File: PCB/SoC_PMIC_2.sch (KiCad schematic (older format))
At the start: 1 part

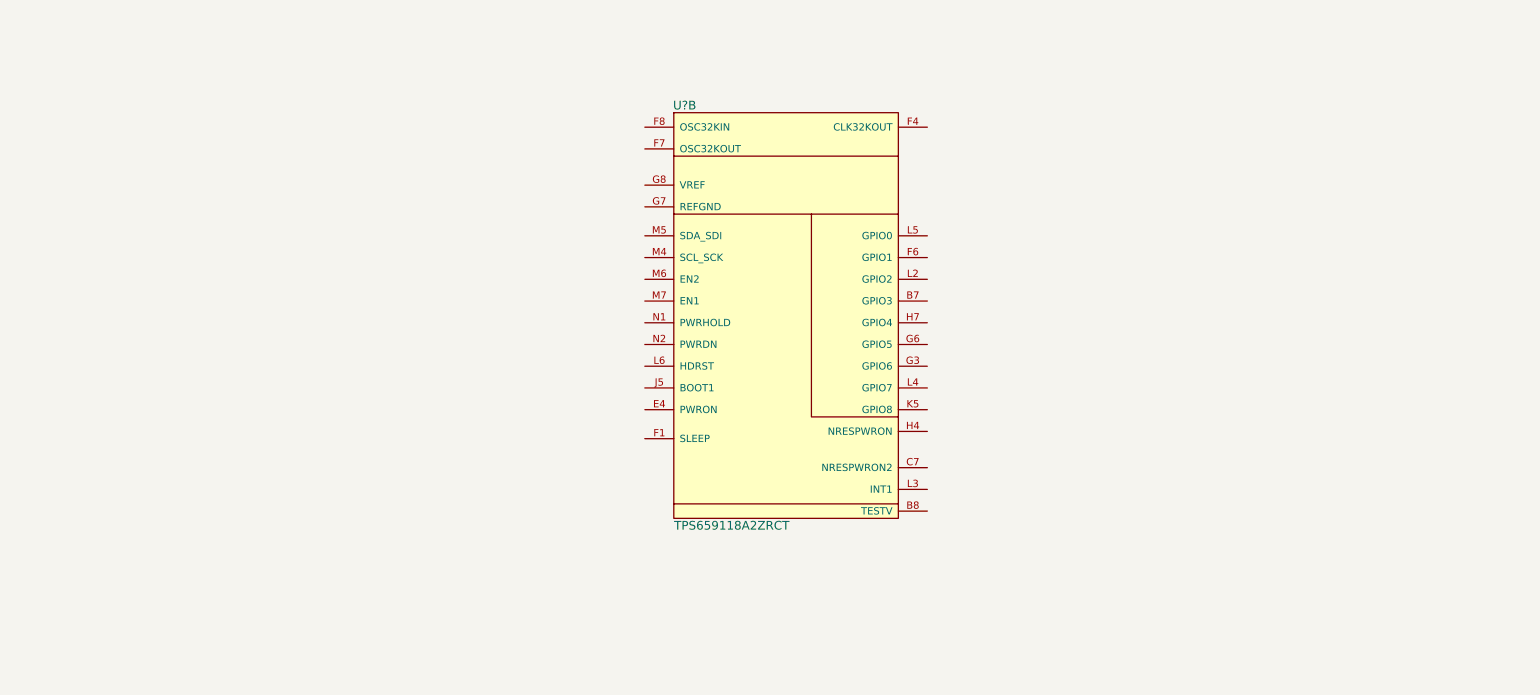
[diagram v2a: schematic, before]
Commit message: Schematic Progress
More progress on schematic. Image sensor schematic nearly finished, need
to check termination requirements of signals. Memory schematic nearly
solidified. LDO added to image sensor circuit for analog supply (3V).
Need to research termination requirements for memory as well. Need to
check what internal termination if any resistors are available in the
Zynq soc.
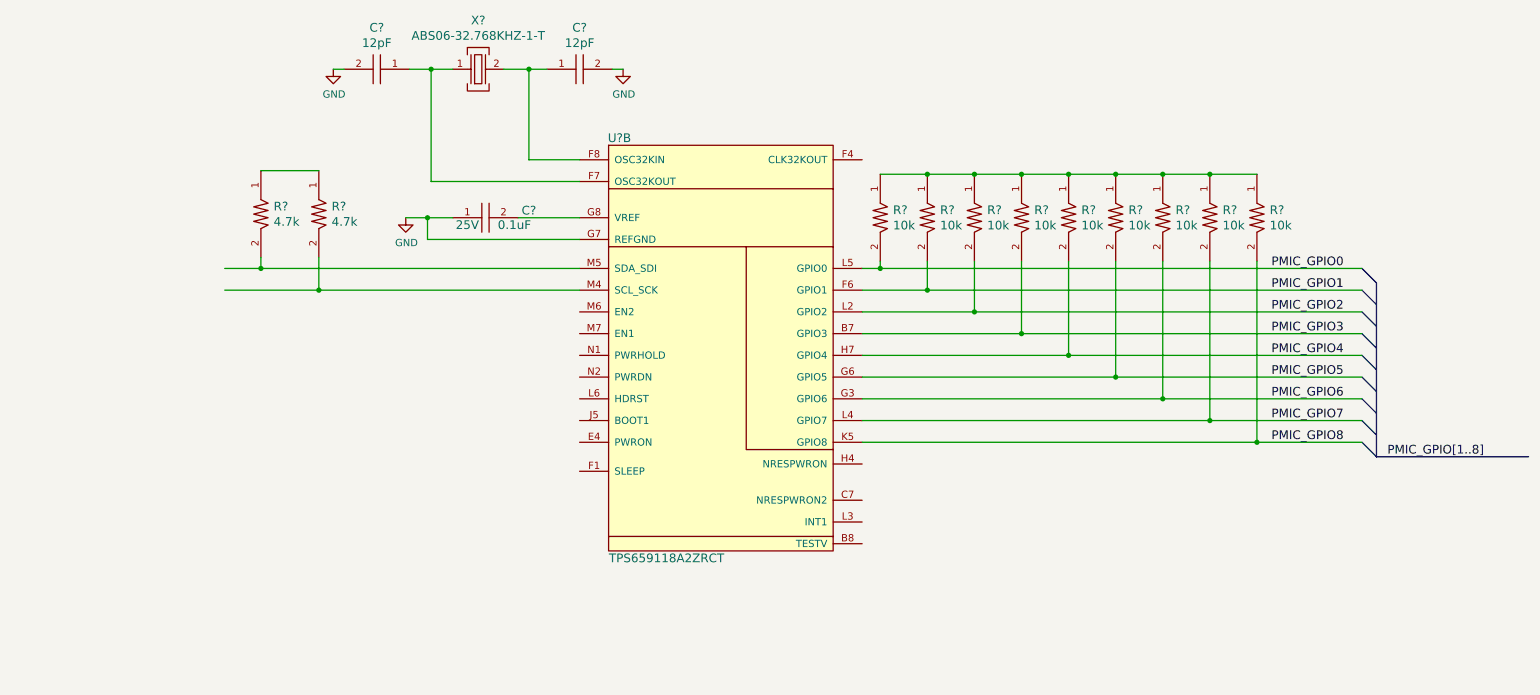
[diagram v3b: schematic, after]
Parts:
- added C? (x2): CL10C120FB8NNNC, PCB_Footprints:C0603, symbol CL10C120FB8NNNC
- added C?: 08053C104JAT2A, PCB_Footprints:C0805, symbol 08053C104JAT2A
- added R? (x9): RC1005F103CS, PCB_Footprints:R0402, symbol RC1005F103CS
- added R? (x2): RC1005F472CS, PCB_Footprints:R0402, symbol RC1005F472CS
- added X?: ABS06-32.768KHZ-1-T, PCB_Footprints:ABS06-32.768KHZ-1-T, symbol ABS06-32.768KHZ-1-T
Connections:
- net labels added: GND, PMIC_GPIO0, PMIC_GPIO1, PMIC_GPIO2, PMIC_GPIO3, PMIC_GPIO4, PMIC_GPIO5, PMIC_GPIO6, PMIC_GPIO7, PMIC_GPIO8, PMIC_GPIO[1..8]
- wire segments 0 -> 36
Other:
- moved on the sheet: U?B

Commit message: Memory and Camera
Memory and Camera schematics tentatively complete. They are subject to
change as all hardware projects are.
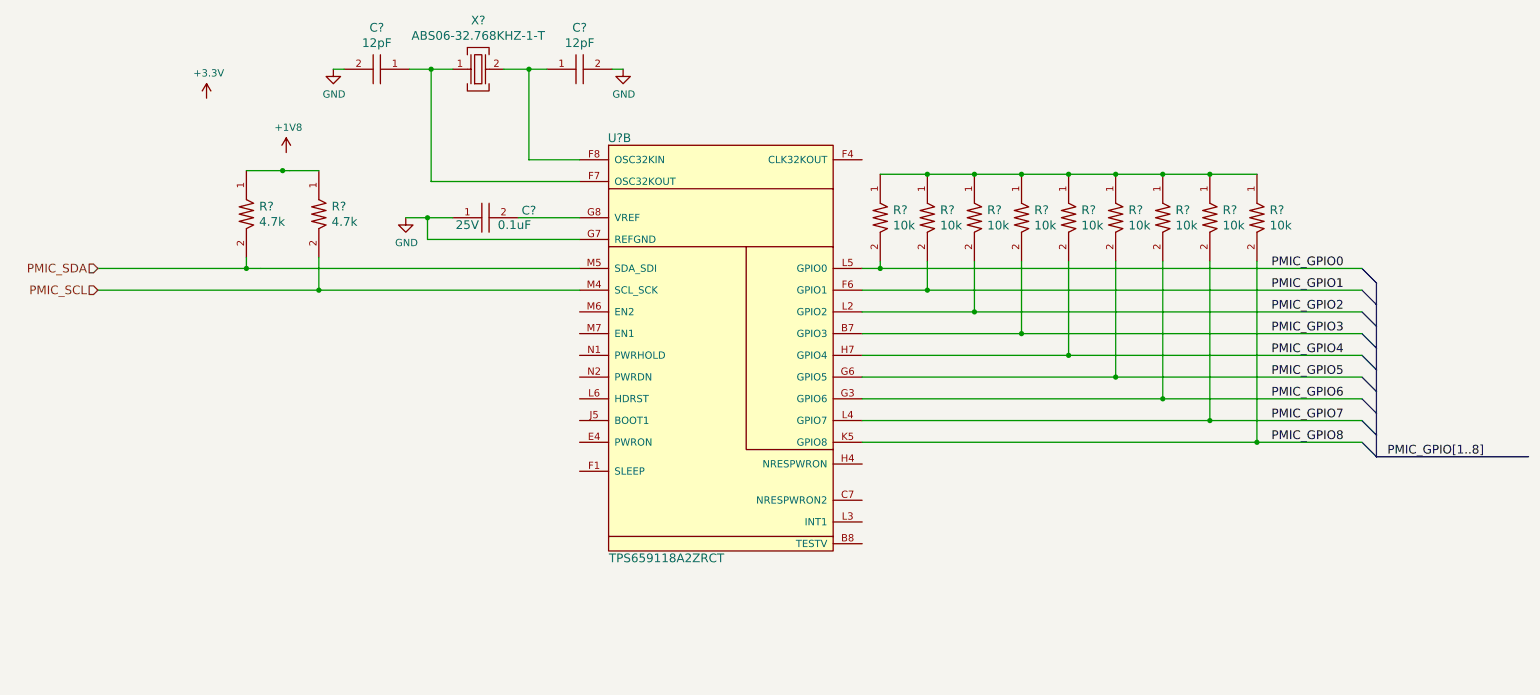
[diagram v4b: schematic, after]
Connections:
- net labels added: +1V8, +3.3V, PMIC_SCL, PMIC_SDA
- wire segments 36 -> 60
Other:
- moved on the sheet: R?
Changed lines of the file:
@@
 $Descr A4 11693 8268
 encoding utf-8
-Sheet 9 9
+Sheet 9 8
 Title ""
 Date ""
@@
 $EndComp
 Wire Wire Line
-	3800 2100 4100 2100
-Wire Wire Line
-	3150 2100 3450 2100
+	3800 2100 3975 2100
+Wire Wire Line
+	3975 2100 4100 2100
+Wire Wire Line
+	3150 2100 3300 2100
+Wire Wire Line
+	3300 2100 3450 2100
 Wire Wire Line
 	2625 2100 2700 2100
@@
 	3275 3275 4325 3275
 Wire Wire Line
-	3125 3125 3450 3125
+	3125 3125 3275 3125
+Wire Wire Line
+	3275 3125 3450 3125
 Wire Wire Line
 	3275 3275 3275 3125
 Connection ~ 3275 3125
 Wire Wire Line
-	4325 3475 1875 3475
-Wire Wire Line
-	4325 3625 1875 3625
-Wire Wire Line
-	6275 3475 9725 3475
-Wire Wire Line
-	6275 3625 9725 3625
-Wire Wire Line
-	6275 3775 9725 3775
-Wire Wire Line
-	6275 3925 9725 3925
-Wire Wire Line
-	6275 4075 9725 4075
-Wire Wire Line
-	6275 4225 9725 4225
-Wire Wire Line
-	6275 4375 9725 4375
-Wire Wire Line
-	6275 4525 9725 4525
-Wire Wire Line
-	6275 4675 9725 4675
+	4325 3475 2125 3475
+Wire Wire Line
+	2125 3475 2025 3475
+Wire Wire Line
+	2025 3475 1000 3475
+Wire Wire Line
+	4325 3625 2525 3625
+Wire Wire Line
+	2525 3625 1000 3625
+Wire Wire Line
+	6275 3475 6400 3475
+Wire Wire Line
+	6400 3475 9725 3475
+Wire Wire Line
+	6275 3625 6725 3625
+Wire Wire Line
+	6725 3625 9725 3625
+Wire Wire Line
+	6275 3775 7050 3775
+Wire Wire Line
+	7050 3775 9725 3775
+Wire Wire Line
+	6275 3925 7375 3925
+Wire Wire Line
+	7375 3925 9725 3925
+Wire Wire Line
+	6275 4075 7700 4075
+Wire Wire Line
+	7700 4075 9725 4075
+Wire Wire Line
+	6275 4225 8025 4225
+Wire Wire Line
+	8025 4225 9725 4225
+Wire Wire Line
+	6275 4375 8350 4375
+Wire Wire Line
+	8350 4375 9725 4375
+Wire Wire Line
+	6275 4525 8675 4525
+Wire Wire Line
+	8675 4525 9725 4525
+Wire Wire Line
+	6275 4675 9000 4675
+Wire Wire Line
+	9000 4675 9725 4675
 Wire Wire Line
 	6400 3425 6400 3475
@@
 Connection ~ 9000 4675
 Wire Wire Line
-	6400 2825 9000 2825
+	6400 2825 6725 2825
+Wire Wire Line
+	6725 2825 7050 2825
+Wire Wire Line
+	7050 2825 7375 2825
+Wire Wire Line
+	7375 2825 7700 2825
+Wire Wire Line
+	7700 2825 8025 2825
+Wire Wire Line
+	8025 2825 8350 2825
+Wire Wire Line
+	8350 2825 8675 2825
+Wire Wire Line
+	8675 2825 9000 2825
 Connection ~ 8675 2825
 Connection ~ 8350 2825
@@
 	9725 4675 9825 4775
 Wire Bus Line
-	9825 3575 9825 4775
+	9825 3575 9825 3725
+Wire Bus Line
+	9825 3725 9825 3875
+Wire Bus Line
+	9825 3875 9825 4025
+Wire Bus Line
+	9825 4025 9825 4175
+Wire Bus Line
+	9825 4175 9825 4325
+Wire Bus Line
+	9825 4325 9825 4475
+Wire Bus Line
+	9825 4475 9825 4625
+Wire Bus Line
+	9825 4625 9825 4775
 Wire Bus Line
 	9825 4775 10875 4775
@@
 L RC1005F472CS R?
 U 1 1 588E2FC1
-P 2125 3100
-F 0 "R?" V 2072 3188 60  0000 L CNN
-F 1 "RC1005F472CS" H 2125 3347 60  0001 C CNN
-F 2 "PCB_Footprints:R0402" H 1725 3350 60  0001 C CNN
-F 3 "https://media.digikey.com/pdf/Data%20Sheets/Samsung%20PDFs/RC_Series_ds.pdf" H 1825 3550 60  0001 C CNN
-F 4 "0.00173 @ 5000" H 3675 5050 60  0001 C CNN "Cost"
-F 5 "5 Sept 2016" H 2025 3650 60  0001 C CNN "Date Created"
-F 6 "5 Sept 2016" H 2125 3750 60  0001 C CNN "Date Modified"
-F 7 "Adam Vadala-Roth" H 2225 3850 60  0001 C CNN "Designer"
-F 8 "0.4mm" H 2325 3950 60  0001 C CNN "Height"
-F 9 "Yes" H 2425 4050 60  0001 C CNN "RHoS?"
-F 10 "Samsung Electro-Mechanics America, Inc." H 2525 4150 60  0001 C CNN "MFR"
-F 11 "RC1005F472CS" H 2625 4250 60  0001 C CNN "MFR#"
-F 12 "SMT/SMD" H 2725 4350 60  0001 C CNN "Mounting"
-F 13 "2" H 2825 4450 60  0001 C CNN "Pin Count#"
-F 14 "Active" H 2925 4550 60  0001 C CNN "Status"
-F 15 "1%" H 3025 4650 60  0001 C CNN "Tolerance"
-F 16 "passive" H 3125 4750 60  0001 C CNN "Type"
-F 17 "N/A" H 3225 4850 60  0001 C CNN "Voltage"
-F 18 "1/16" H 3325 4950 60  0001 C CNN "Wattage"
-F 19 "4.7k" V 2178 3188 60  0000 L CNN "Component-Value"
-F 20 "RES SMD 4.7K OHM 1% 1/16W 0402" H 3525 5150 60  0001 C CNN "Description"
-	1    2125 3100
+P 2025 3100
+F 0 "R?" V 1972 3188 60  0000 L CNN
+F 1 "RC1005F472CS" H 2025 3347 60  0001 C CNN
+F 2 "PCB_Footprints:R0402" H 1625 3350 60  0001 C CNN
+F 3 "https://media.digikey.com/pdf/Data%20Sheets/Samsung%20PDFs/RC_Series_ds.pdf" H 1725 3550 60  0001 C CNN
+F 4 "0.00173 @ 5000" H 3575 5050 60  0001 C CNN "Cost"
+F 5 "5 Sept 2016" H 1925 3650 60  0001 C CNN "Date Created"
+F 6 "5 Sept 2016" H 2025 3750 60  0001 C CNN "Date Modified"
+F 7 "Adam Vadala-Roth" H 2125 3850 60  0001 C CNN "Designer"
+F 8 "0.4mm" H 2225 3950 60  0001 C CNN "Height"
+F 9 "Yes" H 2325 4050 60  0001 C CNN "RHoS?"
+F 10 "Samsung Electro-Mechanics America, Inc." H 2425 4150 60  0001 C CNN "MFR"
+F 11 "RC1005F472CS" H 2525 4250 60  0001 C CNN "MFR#"
+F 12 "SMT/SMD" H 2625 4350 60  0001 C CNN "Mounting"
+F 13 "2" H 2725 4450 60  0001 C CNN "Pin Count#"
+F 14 "Active" H 2825 4550 60  0001 C CNN "Status"
+F 15 "1%" H 2925 4650 60  0001 C CNN "Tolerance"
+F 16 "passive" H 3025 4750 60  0001 C CNN "Type"
+F 17 "N/A" H 3125 4850 60  0001 C CNN "Voltage"
+F 18 "1/16" H 3225 4950 60  0001 C CNN "Wattage"
+F 19 "4.7k" V 2078 3188 60  0000 L CNN "Component-Value"
+F 20 "RES SMD 4.7K OHM 1% 1/16W 0402" H 3425 5150 60  0001 C CNN "Description"
+	1    2025 3100
 	0    1    1    0
 $EndComp
@@
 $EndComp
 Wire Wire Line
-	2125 3400 2125 3475
-Connection ~ 2125 3475
+	2025 3400 2025 3475
+Connection ~ 2025 3475
 Wire Wire Line
 	2525 3400 2525 3625
 Connection ~ 2525 3625
 Wire Wire Line
-	2125 2800 2525 2800
+	2025 2800 2275 2800
+Wire Wire Line
+	2275 2800 2325 2800
+Wire Wire Line
+	2325 2800 2525 2800
+Text HLabel 1000 3475 0    60   Input ~ 0
+PMIC_SDA
+Text HLabel 1000 3625 0    60   Input ~ 0
+PMIC_SCL
+$Comp
+L +3.3V #PWR?
+U 1 1 588E5DBF
+P 1750 2300
+F 0 "#PWR?" H 1750 2150 50  0001 C CNN
+F 1 "+3.3V" H 1765 2473 50  0000 C CNN
+F 2 "" H 1750 2300 50  0001 C CNN
+F 3 "" H 1750 2300 50  0001 C CNN
+	1    1750 2300
+	1    0    0    -1
+$EndComp
+Connection ~ 2275 2800
+$Comp
+L +1V8 #PWR?
+U 1 1 588EDED9
+P 2300 2675
+F 0 "#PWR?" H 2300 2525 50  0001 C CNN
+F 1 "+1V8" H 2315 2848 50  0000 C CNN
+F 2 "" H 2300 2675 50  0001 C CNN
+F 3 "" H 2300 2675 50  0001 C CNN
+	1    2300 2675
+	1    0    0    -1
+$EndComp
 $EndSCHEMATC

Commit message: USB
This commit contains mostly work done to the USB sections. Theres a FTDI
chip for USB coms and programmign and an USB transceiver/PHY for usb
perfipherals or daisychaining devices.  Also the termiantion resistors
have been removed from the memory since termination can be set on DDR
pins of the FPGA with verilog.
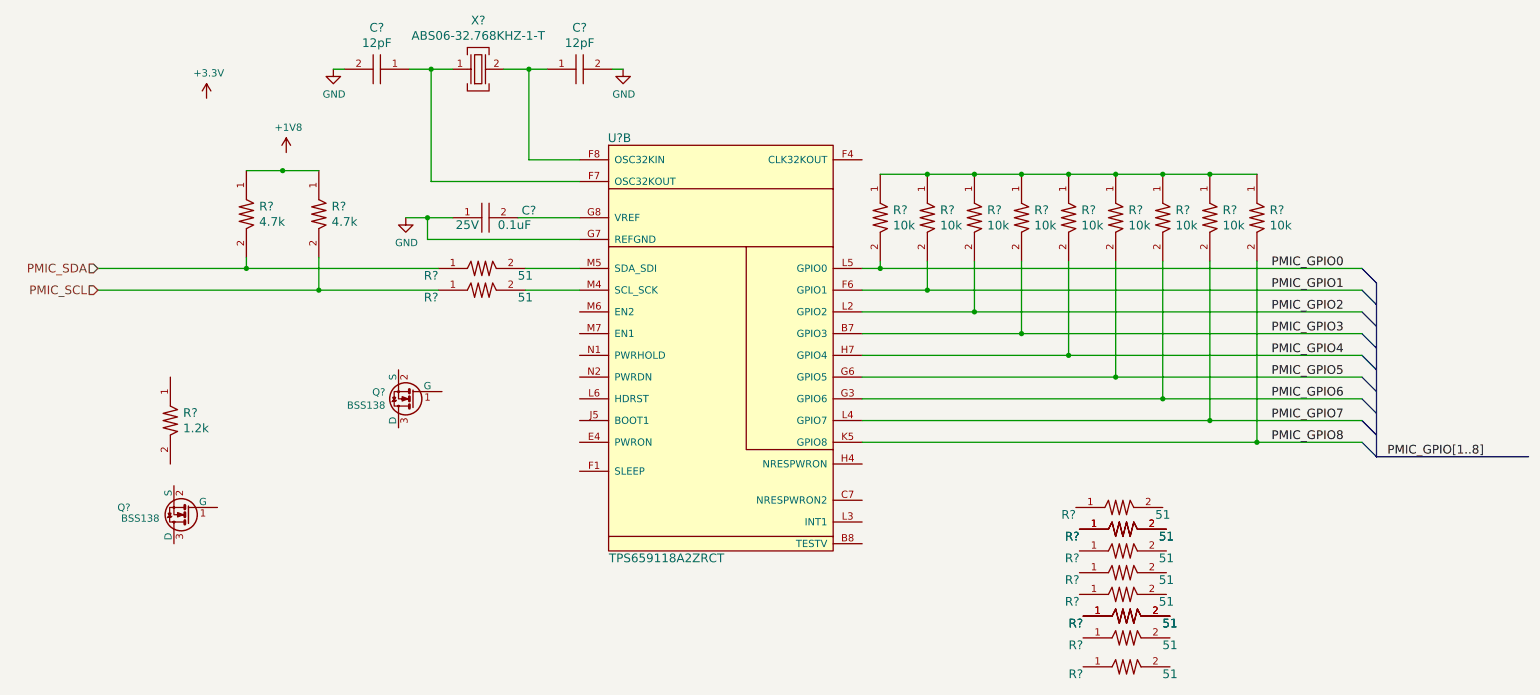
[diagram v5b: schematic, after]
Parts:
- added Q? (x2): BSS138, TO_SOT_Packages_SMD:SOT-23, symbol BSS138
- added R?: ERJ-2RKF1201X, PCB_Footprints:R0402, symbol ERJ-2RKF1201X
- added R? (x12): RC1005F510CS, PCB_Footprints:R0402, symbol RC1005F510CS
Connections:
- wire segments 60 -> 38
